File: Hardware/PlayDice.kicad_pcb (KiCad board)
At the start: 2 copper layers, 40 x 110 mm, 31 parts, among them J1 Clock In, J2 Eurorack_10_pin_power, J3 Action In, J4 OLED, J5 Gate Out, J6 CV Out, Q1 MMBT3904, Q2 MMBT3904, U1 LM1117-5.0, U3 TL072

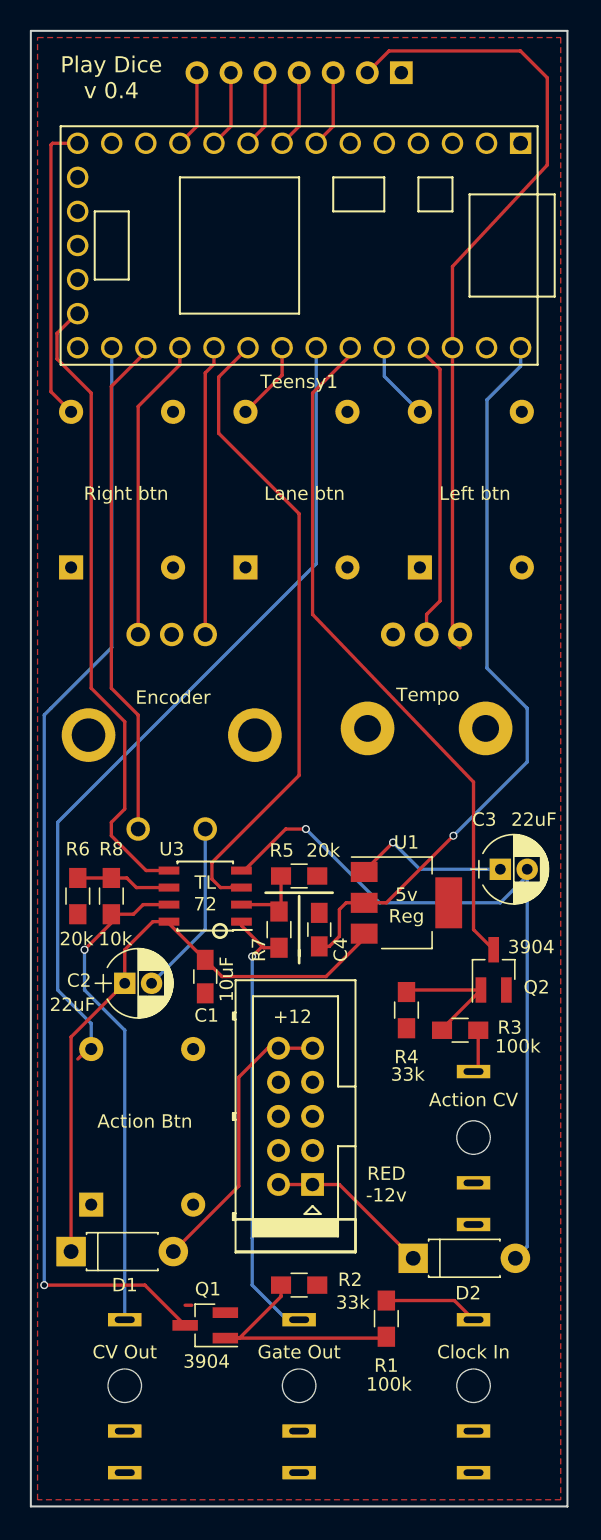
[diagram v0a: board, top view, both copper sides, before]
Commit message: Updated to black and silver colour scheme; Transferred pcb and panel to Kicad 5.99
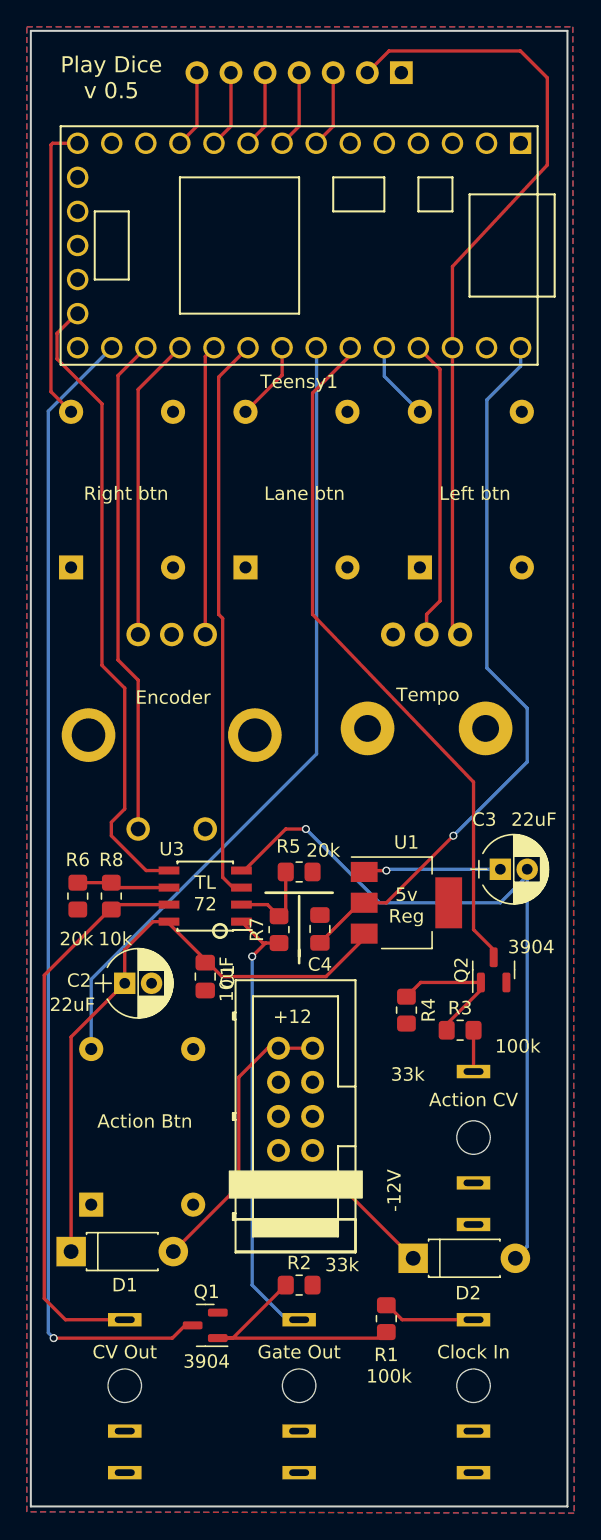
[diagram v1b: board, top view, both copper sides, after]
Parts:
- C1, C4: footprint Capacitors_SMD:C_0805_HandSoldering -> Capacitor_SMD:C_0805_2012Metric_Pad1.18x1.45mm_HandSolder
- J2: footprint Connectors_Multicomp:Multicomp_MC9A12-1034_2x05x2.54mm_Straight -> Custom_Footprints:Eurorack_10_pin_header
- Q1, Q2: footprint TO_SOT_Packages_SMD:SOT-23_Handsoldering -> Package_TO_SOT_SMD:SOT-23
- R1, R2, R3, R4, R5, R6, R7, R8: footprint Resistors_SMD:R_0805_HandSoldering -> Resistor_SMD:R_0805_2012Metric_Pad1.20x1.40mm_HandSolder
- moved R5 0.30 mm to (123.0, 111.7)
- moved C4 0.07 mm to (124.5, 116.0)
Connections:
- net Net-(D1-Pad2) renamed +12V
- net Net-(D2-Pad1) renamed -12V
- Action1 pad 1: (no net) -> unconnected-(Action1-Pad1)
- Action1 pad 4: (no net) -> unconnected-(Action1-Pad4)
- J1 pad 2: Net-(J1-Pad2) -> GND
- J3 pad 2: Net-(J3-Pad2) -> GND
- J5 pad 2: Net-(J5-Pad2) -> unconnected-(J5-Pad2)
- J6 pad 2: Net-(J6-Pad2) -> unconnected-(J6-Pad2)
- Lane1 pad 1: (no net) -> unconnected-(Lane1-Pad1)
- Lane1 pad 4: (no net) -> unconnected-(Lane1-Pad4)
- Left1 pad 1: (no net) -> unconnected-(Left1-Pad1)
- Left1 pad 4: (no net) -> unconnected-(Left1-Pad4)
- Right1 pad 1: (no net) -> unconnected-(Right1-Pad1)
- Right1 pad 4: (no net) -> unconnected-(Right1-Pad4)
- Teensy1 pad 12: Net-(Teensy1-Pad12) -> unconnected-(Teensy1-Pad12)
- Teensy1 pad 15: Net-(Teensy1-Pad15) -> unconnected-(Teensy1-Pad15)
- Teensy1 pad 16: Net-(Teensy1-Pad16) -> unconnected-(Teensy1-Pad16)
- Teensy1 pad 17: Net-(Teensy1-Pad17) -> unconnected-(Teensy1-Pad17)
- Teensy1 pad 18: Net-(Teensy1-Pad18) -> unconnected-(Teensy1-Pad18)
- Teensy1 pad 2: Net-(Teensy1-Pad2) -> unconnected-(Teensy1-Pad2)
- Teensy1 pad 20: Net-(Teensy1-Pad20) -> unconnected-(Teensy1-Pad20)
- Teensy1 pad 3: Net-(Teensy1-Pad3) -> unconnected-(Teensy1-Pad3)
- Teensy1 pad 32: Net-(Teensy1-Pad32) -> unconnected-(Teensy1-Pad32)
- Teensy1 pad 4: Net-(Teensy1-Pad4) -> unconnected-(Teensy1-Pad4)
- Teensy1 pad 5: Net-(Teensy1-Pad5) -> unconnected-(Teensy1-Pad5)
- Teensy1 pad 6: Net-(Teensy1-Pad6) -> unconnected-(Teensy1-Pad6)
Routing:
- net GND: track 25.3 -> 10.1 mm
- net /GATE: track 48.3 -> 42.2 mm
- net Net-(J6-Pad3): track 37.0 -> 41.7 mm, vias 1 -> 0
- net /ACTION: track 62.1 -> 59.3 mm
- net /CLOCK: track 83.7 -> 86.1 mm
- net +5V: track 55.5 -> 53.9 mm
- net Net-(J5-Pad3): track 34.5 -> 33.0 mm
- net VCC: track 46.3 -> 45.3 mm
- net Net-(R5-Pad2): track 5.73 -> 6.67 mm
- net +3V3: track 60.4 -> 59.6 mm
- net VEE: track 55.6 -> 54.8 mm
- net Net-(R6-Pad2): track 7.10 -> 6.44 mm
- net /OLED_D1: track 6.41 -> 5.79 mm
- net /ACTIONCV: track 51.5 -> 50.9 mm
- net (no net): track 0.50 -> 0.00 mm
- added copper zone on B.Cu, net GND
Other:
- board text added: "Play Dice v 0.5"
- board text removed: "Play Dice v 0.4"
- board text removed: "RED -12v"
